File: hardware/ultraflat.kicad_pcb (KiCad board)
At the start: 2 copper layers, 114.5 x 85 mm, 53 parts, among them SW1 SW_Push, SW10 SW_Push, SW11 SW_Push, SW12 SW_Push, SW13 SW_Push, SW14 SW_Push, SW15 SW_Push, SW16 SW_Push, SW17 SW_Push, SW18 SW_Push, SW19 SW_Push, SW2 SW_Push, SW20 SW_Push, SW21 SW_Push, SW22 SW_Push, SW23 SW_Push, SW24 SW_Push, SW25 SW_Push, SW26 SW_Push, SW27 SW_Push, SW28 SW_Push, SW29 SW_Push, SW3 SW_Push, SW30 SW_Push, SW4 SW_Push, SW5 SW_Push, SW6 SW_Push, SW7 SW_Push, SW8 SW_Push, SW9 SW_Push, U1 nRF52840, Y2 32.768kHz

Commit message: Finish most of schem
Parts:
- added C1: 15pF, Capacitor_SMD:C_0402_1005Metric, B.Cu at (105.6, 49.2)
- added C2: 15pF, Capacitor_SMD:C_0402_1005Metric, B.Cu at (109.5, 49.2)
- added C21: 4.7uF, Capacitor_SMD:C_0603_1608Metric, B.Cu at (112.0, 75.8)
- added C22: 4.7uF, Capacitor_SMD:C_0603_1608Metric, B.Cu at (115.3, 69.9)
- added C3: 15pF, Capacitor_SMD:C_0402_1005Metric, B.Cu at (121.7, 54.8)
- added C4: 15pF, Capacitor_SMD:C_0402_1005Metric, B.Cu at (118.4, 56.5)
- added J1: USB_C_Receptacle_USB2.0_14P, Connector_USB:USB_C_Receptacle_HRO_TYPE-C-31-M-12, B.Cu at (157.5, 46.4)
- added J2: Conn_01x02, Connector_PinSocket_2.54mm:PinSocket_1x02_P2.54mm_Vertical, B.Cu at (104.7, 76.4)
- added J3: USB_C_Receptacle_USB2.0_14P, Connector_USB:USB_C_Receptacle_HRO_TYPE-C-31-M-12, B.Cu at (154.2, 143.6)
- added JP1: SolderJumper_2_Open, Jumper:SolderJumper-2_P1.3mm_Open_RoundedPad1.0x1.5mm, B.Cu at (112.7, 66.3)
- added Q2: 2N7002, Package_TO_SOT_SMD:SOT-23, B.Cu at (120.1, 71.0)
- added R1: 5.1k, Resistor_SMD:R_0402_1005Metric_Pad0.72x0.64mm_HandSolder, B.Cu at (151.7, 49.5)
- added R10: 10k, Resistor_SMD:R_0402_1005Metric_Pad0.72x0.64mm_HandSolder, B.Cu at (100.4, 61.1)
- added R11: 5.1k, Resistor_SMD:R_0402_1005Metric_Pad0.72x0.64mm_HandSolder, B.Cu at (150.0, 137.9)
- added R12: 5.1k, Resistor_SMD:R_0402_1005Metric_Pad0.72x0.64mm_HandSolder, B.Cu at (150.0, 135.9)
- added R2: 5.1k, Resistor_SMD:R_0402_1005Metric_Pad0.72x0.64mm_HandSolder, B.Cu at (163.3, 49.5)
- added R3: 10k, Resistor_SMD:R_0402_1005Metric_Pad0.72x0.64mm_HandSolder, B.Cu at (112.4, 63.1)
- added R4: 3.9k, Resistor_SMD:R_0402_1005Metric_Pad0.72x0.64mm_HandSolder, B.Cu at (116.8, 73.6)
- added R5: 1.5k, Resistor_SMD:R_0402_1005Metric_Pad0.72x0.64mm_HandSolder, B.Cu at (113.5, 69.3)
- added R6: 10k, Resistor_SMD:R_0402_1005Metric_Pad0.72x0.64mm_HandSolder, B.Cu at (118.0, 69.9)
- added R7: 100, Resistor_SMD:R_0402_1005Metric_Pad0.72x0.64mm_HandSolder, B.Cu at (122.5, 70.6)
- added R8: 10k, Resistor_SMD:R_0402_1005Metric_Pad0.72x0.64mm_HandSolder, B.Cu at (100.4, 65.1)
- added R9: 1.5k, Resistor_SMD:R_0402_1005Metric_Pad0.72x0.64mm_HandSolder, B.Cu at (110.5, 70.6)
- added U2: BQ24075RGT, Package_DFN_QFN:VQFN-16-1EP_3x3mm_P0.5mm_EP1.6x1.6mm, B.Cu at (112.8, 72.8)
- added Y1: 32MHz 12pF, Crystal:Crystal_SMD_2016-4Pin_2.0x1.6mm, B.Cu at (107.5, 49.2)
- Y2: value 32.768kHz -> 32.768kHz 12.5pF
- moved C11 103.5 mm to (114.7, 49.4)
- moved C12 101.4 mm to (114.9, 50.6)
- moved C18 100.4 mm to (110.0, 50.6), turned to 180 degrees
- moved C10 99.2 mm to (107.2, 56.5)
- moved Y2 97.7 mm to (119.2, 54.8), turned to 180 degrees
- moved C8 94.3 mm to (118.1, 53.0), turned to 180 degrees
- moved L3 94.0 mm to (116.3, 47.6), turned to 180 degrees
- moved C13 88.7 mm to (116.9, 61.5), turned to 90 degrees
- moved C17 88.3 mm to (118.7, 51.8)
- moved L2 88.1 mm to (117.0, 49.5), turned to 90 degrees
- moved C19 87.8 mm to (112.4, 61.0), turned to -90 degrees
- moved C20 86.6 mm to (109.4, 61.0), turned to -90 degrees
- moved C14 86.3 mm to (115.4, 61.5), turned to -90 degrees
- moved C15 85.9 mm to (118.7, 59.1)
- moved C16 84.9 mm to (118.7, 57.6)
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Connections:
- SW1 pad MP: (no net) -> GND
- SW10 pad MP: (no net) -> GND
- SW11 pad MP: (no net) -> GND
- SW12 pad MP: (no net) -> GND
- SW13 pad MP: (no net) -> GND
- SW14 pad MP: (no net) -> GND
- SW15 pad MP: (no net) -> GND
- SW16 pad MP: (no net) -> GND
- SW17 pad MP: (no net) -> GND
- SW18 pad MP: (no net) -> GND
- SW19 pad MP: (no net) -> GND
- SW2 pad MP: (no net) -> GND
- SW20 pad MP: (no net) -> GND
- SW21 pad MP: (no net) -> GND
- SW22 pad MP: (no net) -> GND
- SW23 pad MP: (no net) -> GND
- SW24 pad MP: (no net) -> GND
- SW25 pad MP: (no net) -> GND
- SW26 pad MP: (no net) -> GND
- SW27 pad MP: (no net) -> GND
- SW28 pad MP: (no net) -> GND
- SW29 pad MP: (no net) -> GND
- SW3 pad MP: (no net) -> GND
- SW30 pad MP: (no net) -> GND
- SW4 pad MP: (no net) -> GND
- SW5 pad MP: (no net) -> GND
- SW6 pad MP: (no net) -> GND
- SW7 pad MP: (no net) -> GND
- SW8 pad MP: (no net) -> GND
- SW9 pad MP: (no net) -> GND
- U1 pad AC13: unconnected-(U1-P0.18/~{RESET}-PadAC13) -> /~{RESET}
- U1 pad AD12: unconnected-(U1-P0.17-PadAD12) -> /~{RESET}
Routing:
- net /D+: track 0.00 -> 59.7 mm
- net /D-: track 0.00 -> 58.3 mm
- net VDD_nRF: track 0.00 -> 29.6 mm, vias 0 -> 6
- net +BATT: track 0.00 -> 12.5 mm
- net Net-(J1-CC1): track 0.00 -> 7.64 mm, vias 0 -> 2
- net /~{RESET}: track 0.00 -> 7.57 mm
- net Net-(U1-XL1/P0.00): track 0.00 -> 6.94 mm
- net Net-(U1-XC1): track 0.00 -> 6.50 mm
- net Net-(J1-CC2): track 0.00 -> 6.07 mm, vias 0 -> 2
- net /SYSOFF: track 0.00 -> 5.78 mm
- net Net-(U1-DEC4): track 10.1 -> 15.2 mm
- net Net-(U1-XC2): track 0.00 -> 5.11 mm
- net Net-(U1-XL2/P0.01): track 0.00 -> 4.54 mm
- net Net-(U1-DCCH): track 0.00 -> 4.14 mm
- net Net-(Q2-G): track 0.00 -> 3.89 mm
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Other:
- board size 114.5 x 85 mm -> 113.7 x 85 mm

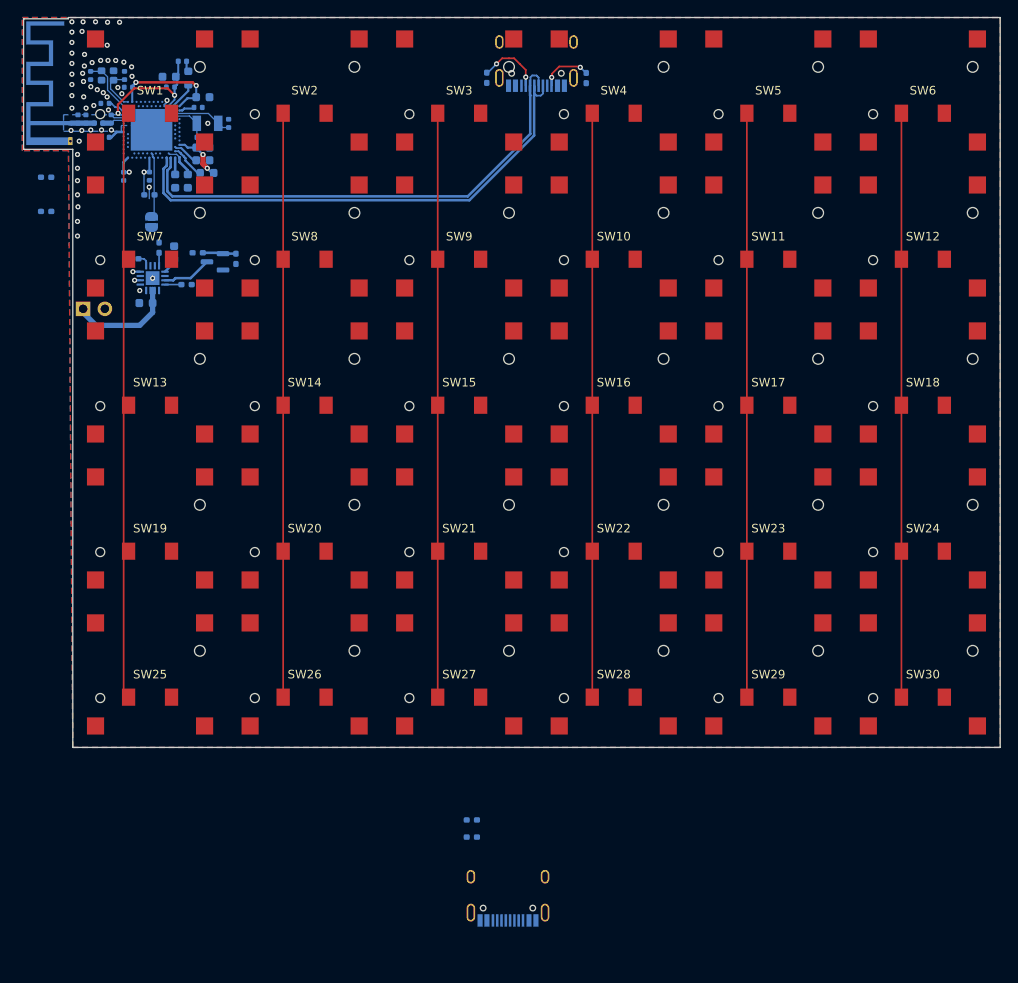
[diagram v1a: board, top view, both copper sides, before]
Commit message: 2 Layers
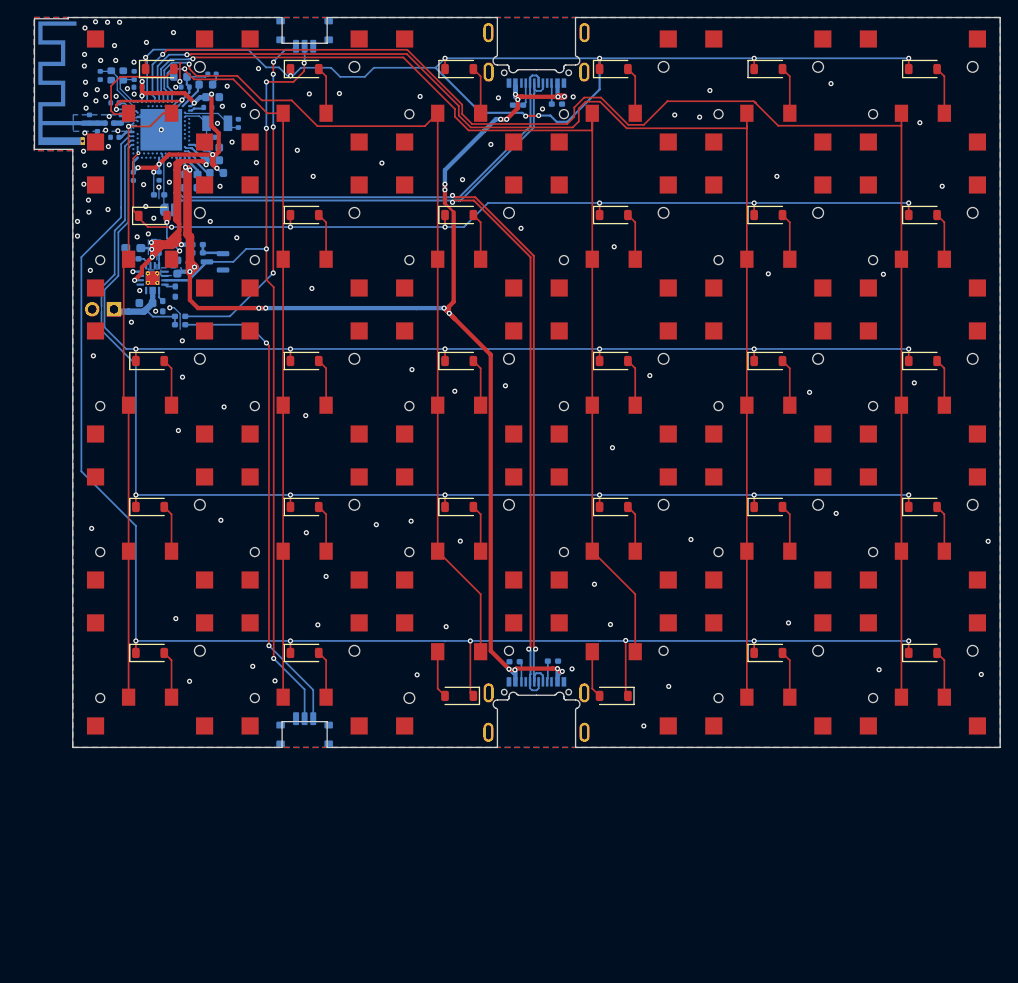
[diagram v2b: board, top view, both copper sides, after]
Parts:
- added D1: 1N4148W, Diode_SMD:D_SOD-123, F.Cu at (130.5, 48.5)
- added D10: 1N4148W, Diode_SMD:D_SOD-123, F.Cu at (184.5, 65.5)
- added D11: 1N4148W, Diode_SMD:D_SOD-123, F.Cu at (202.5, 65.5)
- added D12: 1N4148W, Diode_SMD:D_SOD-123, F.Cu at (112.5, 82.5)
- added D13: 1N4148W, Diode_SMD:D_SOD-123, F.Cu at (130.5, 82.5)
- added D14: 1N4148W, Diode_SMD:D_SOD-123, F.Cu at (148.5, 82.5)
- added D15: 1N4148W, Diode_SMD:D_SOD-123, F.Cu at (166.5, 82.5)
- added D16: 1N4148W, Diode_SMD:D_SOD-123, F.Cu at (184.5, 82.5)
- added D17: 1N4148W, Diode_SMD:D_SOD-123, F.Cu at (202.5, 82.5)
- added D18: 1N4148W, Diode_SMD:D_SOD-123, F.Cu at (112.5, 99.5)
- added D19: 1N4148W, Diode_SMD:D_SOD-123, F.Cu at (130.5, 99.5)
- added D2: 1N4148W, Diode_SMD:D_SOD-123, F.Cu at (148.5, 48.5)
- added D20: 1N4148W, Diode_SMD:D_SOD-123, F.Cu at (148.5, 99.5)
- added D21: 1N4148W, Diode_SMD:D_SOD-123, F.Cu at (166.5, 99.5)
- added D22: 1N4148W, Diode_SMD:D_SOD-123, F.Cu at (184.5, 99.5)
- added D23: 1N4148W, Diode_SMD:D_SOD-123, F.Cu at (202.5, 99.5)
- added D24: 1N4148W, Diode_SMD:D_SOD-123, F.Cu at (112.5, 116.5)
- added D25: 1N4148W, Diode_SMD:D_SOD-123, F.Cu at (130.5, 116.5)
- added D26: 1N4148W, Diode_SMD:D_SOD-123, F.Cu at (148.5, 121.5)
- added D27: 1N4148W, Diode_SMD:D_SOD-123, F.Cu at (166.5, 121.5)
- added D28: 1N4148W, Diode_SMD:D_SOD-123, F.Cu at (184.5, 116.5)
- added D29: 1N4148W, Diode_SMD:D_SOD-123, F.Cu at (202.5, 116.5)
- added D3: 1N4148W, Diode_SMD:D_SOD-123, F.Cu at (166.5, 48.5)
- added D31: LED, LED_SMD:LED_0603_1608Metric_Pad1.05x0.95mm_HandSolder, B.Cu at (110.5, 69.3)
- added D32: 1N4148W, Diode_SMD:D_SOD-123, F.Cu at (113.6, 48.5)
- added D4: 1N4148W, Diode_SMD:D_SOD-123, F.Cu at (184.5, 48.5)
- added D5: 1N4148W, Diode_SMD:D_SOD-123, F.Cu at (202.5, 48.5)
- added D6: 1N4148W, Diode_SMD:D_SOD-123, F.Cu at (112.8, 65.6)
- added D7: 1N4148W, Diode_SMD:D_SOD-123, F.Cu at (130.5, 65.5)
- added D8: 1N4148W, Diode_SMD:D_SOD-123, F.Cu at (148.5, 65.5)
- added D9: 1N4148W, Diode_SMD:D_SOD-123, F.Cu at (166.5, 65.5)
- added R13: 10k, Resistor_SMD:R_0402_1005Metric_Pad0.72x0.64mm_HandSolder, B.Cu at (116.0, 78.3)
- added SW31: SW_SPDT, ultraflat:Switch_Sink_MINI_MSK12CO2, B.Cu at (130.5, 44.0)
- added SW32: SW_SPDT, ultraflat:Switch_Sink_MINI_MSK12CO2, B.Cu at (130.5, 126.0)
- J1, J3: footprint Connector_USB:USB_C_Receptacle_HRO_TYPE-C-31-M-12 -> PCM_marbastlib-various:USB_C_Receptacle_HRO_TYPE-C-31-M-14
- U2: footprint Package_DFN_QFN:VQFN-16-1EP_3x3mm_P0.5mm_EP1.6x1.6mm -> Package_DFN_QFN:VQFN-16-1EP_3x3mm_P0.5mm_EP1.6x1.6mm_ThermalVias
- moved J3 22.8 mm to (157.5, 121.1), turned to 180 degrees
- moved R11 22.6 mm to (159.4, 117.5)
- moved R10 20.3 mm to (114.0, 76.1), turned to 90 degrees
- moved R8 19.8 mm to (116.0, 77.3), turned to 180 degrees
- moved R12 19.1 mm to (154.9, 117.5), turned to 180 degrees
- moved R1 4.83 mm to (155.3, 52.7), turned to 180 degrees
- moved R7 4.75 mm to (118.0, 69.0), turned to 180 degrees
- moved R2 4.56 mm to (159.9, 52.6), turned to 0 degrees
- moved L3 3.76 mm to (119.7, 49.1)
- moved J2 3.60 mm to (108.3, 76.5), turned to 90 degrees
- moved JP1 2.54 mm to (114.8, 64.9), turned to 180 degrees
- moved J1 2.54 mm to (157.5, 48.9)
- moved L2 2.19 mm to (119.0, 50.3), turned to 0 degrees
- moved C12 1.72 mm to (116.6, 50.6)
- moved C22 1.70 mm to (115.7, 71.6)
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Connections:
- net Net-(U1-DEC1) renamed /DEC1
- net Net-(U1-DEC3) renamed /DEC3
- net Net-(U1-DEC4) renamed /DEC4_6
- net Net-(U1-DEC5) renamed /DEC5
- net Net-(U1-DECUSB) renamed /DECUSB
- C15 pad 1: VDDH -> +5V
- SW1 pad 1: /COL0 -> Net-(D32-A)
- SW1 pad 2: Net-(D1-A) (its old number) -> /COL0
- U1 pad A10: unconnected-(U1-AIN5/P0.29-PadA10) -> /COL2
- U1 pad A12: unconnected-(U1-AIN0/P0.02-PadA12) -> /COL3
- U1 pad A14: unconnected-(U1-P1.15-PadA14) -> /COL4
- U1 pad A16: unconnected-(U1-P1.13-PadA16) -> /COL5
- U1 pad A20: unconnected-(U1-P1.10-PadA20) -> /ROW0
- U1 pad A8: unconnected-(U1-AIN7/P0.31-PadA8) -> /COL1
- U1 pad J24: unconnected-(U1-NFC2/P0.10-PadJ24) -> /COL0
- U1 pad R24: unconnected-(U1-P1.06-PadR24) -> /ROW4
- U1 pad U24: unconnected-(U1-P1.04-PadU24) -> /ROW3
- U1 pad W24: unconnected-(U1-P1.02-PadW24) -> /ROW2
- U1 pad Y2: VDDH -> +5V
- U1 pad Y23: unconnected-(U1-P1.01-PadY23) -> /ROW1
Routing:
- net /ROW4: track 0.00 -> 172.9 mm, vias 0 -> 6
- net VBUS: track 3.81 -> 156.1 mm, vias 0 -> 20
- net /ROW3: track 0.00 -> 142.4 mm, vias 0 -> 6
- net /ROW0: track 0.00 -> 131.9 mm, vias 0 -> 8
- net /ROW2: track 0.00 -> 125.8 mm, vias 0 -> 6
- net /ROW1: track 0.00 -> 107.1 mm, vias 0 -> 7
- net /COL5: track 68.0 -> 170.2 mm, vias 0 -> 1
- net /SYSOFF: track 5.78 -> 97.2 mm, vias 0 -> 5
- net /COL4: track 68.0 -> 149.3 mm, vias 0 -> 1
- net /D-: track 58.3 -> 121.3 mm, vias 0 -> 2
- net /D+: track 59.7 -> 121.7 mm, vias 0 -> 2
- net /COL3: track 68.0 -> 125.5 mm, vias 0 -> 1
- net Net-(SW32-A): track 0.00 -> 56.3 mm, vias 0 -> 2
- net +5V: track 0.66 -> 54.2 mm, vias 1 -> 6
- net Net-(SW31-A): track 0.00 -> 40.4 mm, vias 0 -> 4
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- added copper zone on B.Cu, net +5V
- added copper zone on B.Cu, net VBUS
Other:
- board size 113.7 x 85 mm -> 112.5 x 85 mm

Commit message: Case
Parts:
- added TP1: TestPoint, TestPoint:TestPoint_Pad_D1.5mm, B.Cu at (109.1, 63.0)
- added TP2: TestPoint, TestPoint:TestPoint_Pad_D1.5mm, B.Cu at (109.1, 65.5)
- added TP3: TestPoint, TestPoint:TestPoint_Pad_D1.5mm, B.Cu at (119.3, 74.8)
- added TP4: TestPoint, TestPoint:TestPoint_Pad_D1.5mm, B.Cu at (112.7, 79.1)
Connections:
- U1 pad AA24: unconnected-(U1-SWDCLK-PadAA24) -> Net-(U1-SWDCLK)
- U1 pad AC24: unconnected-(U1-SWDIO-PadAC24) -> Net-(U1-SWDIO)
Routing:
- net Net-(U1-SWDIO): track 0.00 -> 8.26 mm
- net Net-(U1-SWDCLK): track 0.00 -> 5.85 mm
- net VBUS: track 156.1 -> 158.2 mm, vias 20 -> 21
- net /SYSOFF: track 97.2 -> 97.9 mm
- net GND: vias 123 -> 133
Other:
- board size 112.5 x 85 mm -> 112.3 x 85 mm
- board text added: "+"
